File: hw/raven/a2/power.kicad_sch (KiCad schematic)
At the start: 28 parts, among them J201 ATX Power, J202 Pinhdr_02x04, J203 Pinhdr_01x03, J204 FanHeader, J205 FanHeader, J206 FanHeader, SW201 SW_Push, SW202 SW_Push, U201 LM7905CT_NOPB, U202 MAX16054AZT+T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

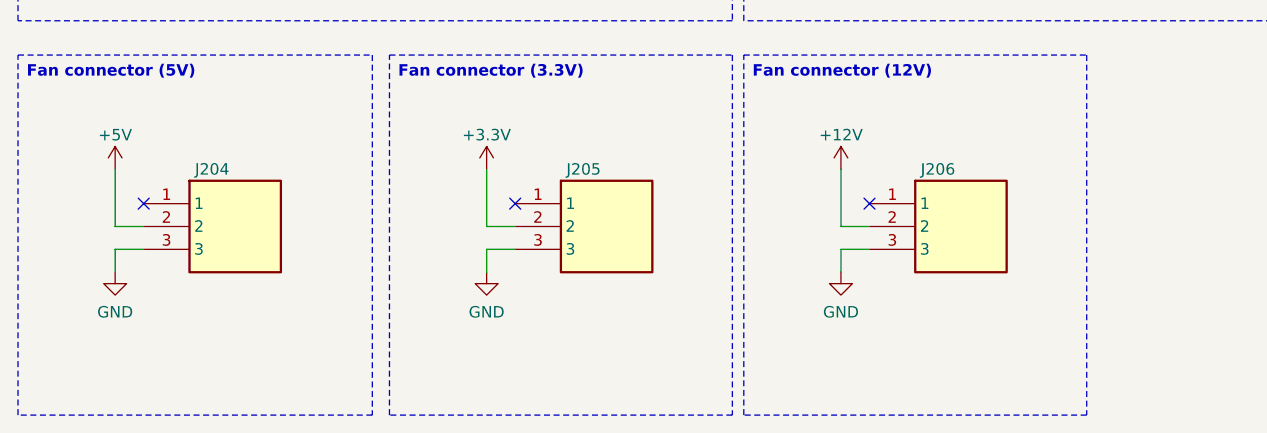
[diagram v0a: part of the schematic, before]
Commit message: A2 wip
audio hooked up
added caps for fan headers
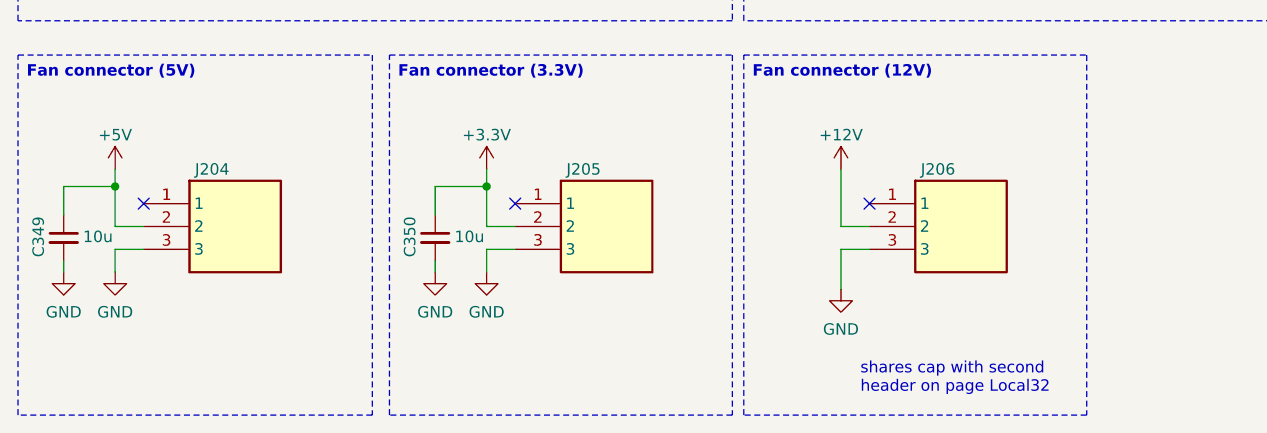
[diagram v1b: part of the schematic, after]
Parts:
- added C349, C350: 10u, Capacitor_SMD:C_1206_3216Metric_Pad1.33x1.80mm_HandSolder, symbol 68k:c_100nf_smd1206
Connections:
- net +3.3V: now also C350.1
- net +5V: now also C349.1
- net GND: now also C349.2, C350.2
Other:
- note added: "shares cap with second header on page Local32"

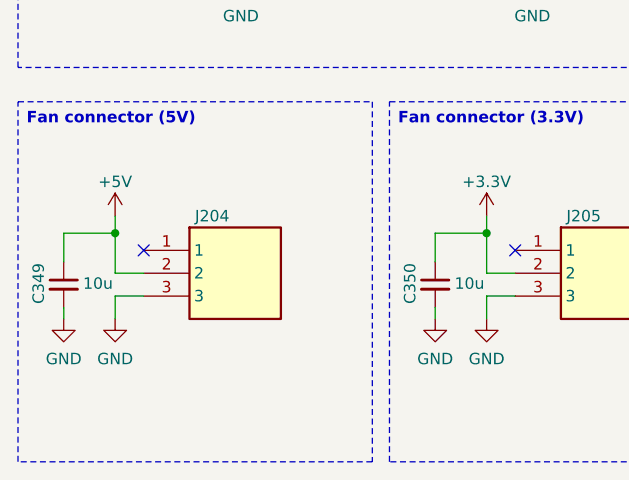
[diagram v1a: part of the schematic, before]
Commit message: A2: changed oscillator caps
also fixed reference identifier
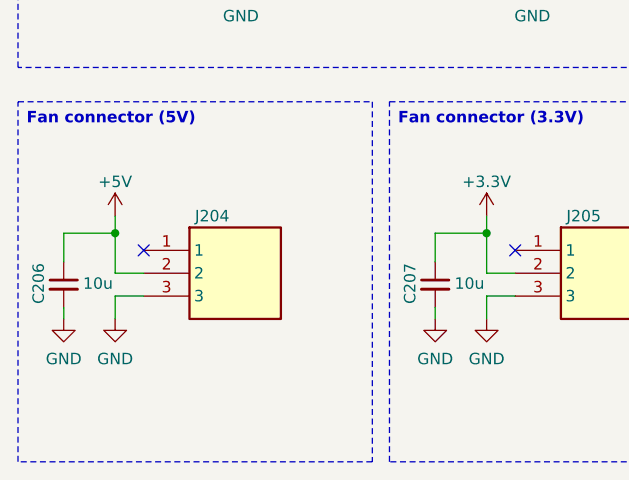
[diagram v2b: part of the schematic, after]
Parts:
- renumbered C349 to C206, C350 to C207
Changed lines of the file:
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@@
 		(dnp no)
 		(fields_autoplaced yes)
-		(property "Reference" "#PWR0240"
+		(property "Reference" "#PWR0237"
 			(at 69.85 178.435 0)
 			(effects
@@
 			(project "raven"
 				(path "/af55e73e-5814-45b4-ac5c-0bab62c0b1c7/3edf683f-0a35-4a7c-880a-e714e6e1adf2"
-					(reference "#PWR0240")
+					(reference "#PWR0237")
 					(unit 1)
 				)
@@
 		(dnp no)
 		(fields_autoplaced yes)
-		(property "Reference" "#PWR0238"
+		(property "Reference" "#PWR0239"
 			(at 114.935 180.34 0)
 			(effects
@@
 			(project "raven"
 				(path "/af55e73e-5814-45b4-ac5c-0bab62c0b1c7/3edf683f-0a35-4a7c-880a-e714e6e1adf2"
-					(reference "#PWR0238")
+					(reference "#PWR0239")
 					(unit 1)
 				)
@@
 		(dnp no)
 		(fields_autoplaced yes)
-		(property "Reference" "#PWR0239"
+		(property "Reference" "#PWR0235"
 			(at 28.575 178.435 0)
 			(effects
@@
 			(project "raven"
 				(path "/af55e73e-5814-45b4-ac5c-0bab62c0b1c7/3edf683f-0a35-4a7c-880a-e714e6e1adf2"
-					(reference "#PWR0239")
+					(reference "#PWR0235")
 					(unit 1)
 				)
@@
 		(dnp no)
 		(fields_autoplaced yes)
-		(property "Reference" "#PWR0235"
+		(property "Reference" "#PWR0236"
 			(at 34.29 178.435 0)
 			(effects
@@
 			(project "raven"
 				(path "/af55e73e-5814-45b4-ac5c-0bab62c0b1c7/3edf683f-0a35-4a7c-880a-e714e6e1adf2"
-					(reference "#PWR0235")
+					(reference "#PWR0236")
 					(unit 1)
 				)
@@
 		(on_board yes)
 		(dnp no)
-		(property "Reference" "C349"
+		(property "Reference" "C206"
 			(at 25.781 168.148 90)
 			(effects
@@
 			(project "raven"
 				(path "/af55e73e-5814-45b4-ac5c-0bab62c0b1c7/3edf683f-0a35-4a7c-880a-e714e6e1adf2"
-					(reference "C349")
+					(reference "C206")
 					(unit 1)
 				)
@@
 		(dnp no)
 		(fields_autoplaced yes)
-		(property "Reference" "#PWR0236"
+		(property "Reference" "#PWR0238"
 			(at 75.565 178.435 0)
 			(effects
@@
 			(project "raven"
 				(path "/af55e73e-5814-45b4-ac5c-0bab62c0b1c7/3edf683f-0a35-4a7c-880a-e714e6e1adf2"
-					(reference "#PWR0236")
+					(reference "#PWR0238")
 					(unit 1)
 				)
@@
 		(on_board yes)
 		(dnp no)
-		(property "Reference" "C350"
+		(property "Reference" "C207"
 			(at 67.056 168.148 90)
 			(effects
@@
 			(project "raven"
 				(path "/af55e73e-5814-45b4-ac5c-0bab62c0b1c7/3edf683f-0a35-4a7c-880a-e714e6e1adf2"
-					(reference "C350")
+					(reference "C207")
 					(unit 1)
 				)

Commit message: misc a2 work
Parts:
- J204, J205, J206: footprint HDRV3W99P0X254_1X3_747X635X843P -> 68k:HDRV3W99P0X254_1X3_747X635X843P
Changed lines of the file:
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@@
 			)
 		)
-		(property "Footprint" "HDRV3W99P0X254_1X3_747X635X843P"
+		(property "Footprint" "68k:HDRV3W99P0X254_1X3_747X635X843P"
 			(at 53.975 259.385 0)
 			(effects
@@
 			)
 		)
-		(property "Footprint" "HDRV3W99P0X254_1X3_747X635X843P"
+		(property "Footprint" "68k:HDRV3W99P0X254_1X3_747X635X843P"
 			(at 95.25 259.385 0)
 			(effects
@@
 			)
 		)
-		(property "Footprint" "HDRV3W99P0X254_1X3_747X635X843P"
+		(property "Footprint" "68k:HDRV3W99P0X254_1X3_747X635X843P"
 			(at 134.62 259.385 0)
 			(effects

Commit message: cosmetic
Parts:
- U201: value LM7905CT_NOPB -> LM7905CT
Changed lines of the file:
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@@
 		(dnp no)
 		(property "Reference" "SW202"
-			(at 84.455 122.555 90)
+			(at 78.486 123.952 0)
 			(effects
 				(font
@@
 					(size 1.27 1.27)
 				)
+				(hide yes)
 			)
 		)
@@
 		)
 		(property "Value" "+3.3V"
-			(at 64.135 88.9 90)
+			(at 64.262 91.186 0)
 			(effects
 				(font
@@
 			)
 		)
-		(property "Value" "LM7905CT_NOPB"
-			(at 224.79 29.21 0)
+		(property "Value" "LM7905CT"
+			(at 224.028 42.672 0)
 			(effects
 				(font
@@
 		(dnp no)
 		(property "Reference" "SW201"
-			(at 59.69 47.625 90)
+			(at 52.832 48.768 0)
 			(effects
 				(font
@@
 				)
 				(justify right)
+				(hide yes)
 			)
 		)
@@
 		(dnp no)
 		(property "Reference" "U202"
-			(at 63.5 34.925 0)
+			(at 62.992 34.798 0)
 			(effects
 				(font
@@
 		(dnp no)
 		(property "Reference" "C201"
-			(at 78.74 29.21 90)
+			(at 82.55 27.686 90)
 			(effects
 				(font
@@
 		)
 		(property "Value" "0.1u"
-			(at 85.09 29.21 90)
+			(at 82.296 33.274 90)
 			(effects
 				(font
@@
 		(dnp no)
 		(property "Reference" "C204"
-			(at 127 95.25 90)
+			(at 130.556 93.726 90)
 			(effects
 				(font
@@
 		)
 		(property "Value" "0.1u"
-			(at 133.35 95.25 90)
+			(at 130.556 99.314 90)
 			(effects
 				(font
@@
 		)
 		(property "Value" "1A 50V"
-			(at 215.9 71.12 0)
+			(at 215.9 71.882 0)
 			(effects
 				(font
@@
 		(dnp no)
 		(property "Reference" "C206"
-			(at 25.781 168.148 90)
+			(at 31.242 166.116 0)
 			(effects
 				(font
@@
 		)
 		(property "Value" "10u"
-			(at 32.385 168.148 0)
+			(at 30.734 170.434 0)
 			(effects
 				(font
@@
 		(dnp no)
 		(property "Reference" "J201"
-			(at 114.3 40.64 0)
+			(at 115.316 40.64 0)
 			(effects
 				(font
@@
 		)
 		(property "Value" "ATX Power"
-			(at 127 40.64 0)
+			(at 130.302 68.834 0)
 			(effects
 				(font
@@
 		)
 		(property "Value" "DS1818"
-			(at 57.15 102.235 0)
+			(at 57.15 123.19 0)
 			(effects
 				(font
@@
 		(dnp no)
 		(property "Reference" "U204"
-			(at 118.11 102.235 0)
+			(at 112.522 114.046 90)
 			(effects
 				(font
@@
 		)
 		(property "Value" "74HCT10"
-			(at 112.395 111.125 0)
+			(at 119.888 115.316 90)
 			(effects
 				(font
@@
 		)
 		(property "Value" "1A 50V"
-			(at 224.79 71.12 0)
+			(at 224.79 71.882 0)
 			(effects
 				(font
@@
 		)
 		(property "Value" "1A 50V"
-			(at 207.01 71.12 0)
+			(at 207.264 71.882 0)
 			(effects
 				(font
@@
 		(dnp no)
 		(property "Reference" "C207"
-			(at 67.056 168.148 90)
+			(at 72.644 166.37 0)
 			(effects
 				(font
@@
 		)
 		(property "Value" "10u"
-			(at 73.66 168.148 0)
+			(at 72.136 170.18 0)
 			(effects
 				(font

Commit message: A2: cosmetics and bom preparations
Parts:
- R202, R203: value 470 -> 220; Manufacturer_Part_Number RT1206FRE07470RL -> RT1206FRE07220RL
- SW201, SW202: value SW_Push -> Button
- U201: value LM7905CT -> LM7905
- U202: value MAX16054AZT+T -> MAX16054
- U204: Manufacturer_Name TI -> Texas Instruments
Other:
- note added: "~13mA 2V"
- note removed: "~6mA 2V"

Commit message: A2: bom
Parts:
- C206, C207: Manufacturer_Part_Number C1206C106K4RAC -> C1206C106K4RACTU
- J203: value Pinhdr_01x03 -> PinHdr_01x03
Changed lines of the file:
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@@
 			)
 		)
-		(property "Value" "Pinhdr_01x03"
+		(property "Value" "PinHdr_01x03"
 			(at 194.945 123.19 0)
 			(effects
@@
 			)
 		)
-		(property "Manufacturer_Part_Number" " C1206C106K4RAC"
+		(property "Manufacturer_Part_Number" " C1206C106K4RACTU"
 			(at 0.635 188.595 0)
 			(effects
@@
 			)
 		)
-		(property "Manufacturer_Part_Number" " C1206C106K4RAC"
+		(property "Manufacturer_Part_Number" " C1206C106K4RACTU"
 			(at 41.91 188.595 0)
 			(effects
